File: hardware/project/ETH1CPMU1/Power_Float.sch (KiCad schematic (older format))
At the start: 53 parts, among them U601 TEL10-2415, U602 MC7815ABD2TR4G, U603 LM1117IMP-3.3/NOPB, U604 TSR1-2450, U605 LT8330_S6, U606 MC7915BD2TG, U607 LM1117IMP-5.0/NOPB, U608 TSR1-2490, U609 LT8330_S6

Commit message: Schematic design
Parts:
- added C628: 22u/16V, Capacitor_SMD:C_2220_5650Metric_Pad1.97x5.40mm_HandSolder, symbol Device:C
- added U610: LM1117IMP-3.3/NOPB, Package_TO_SOT_SMD:SOT-223-3_TabPin2, symbol Regulator_Linear:LM1117-3.3
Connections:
- net AGNDF: now also D602.1 (K), C628.2, U610.1 (GND)
- net at C609.1, U603.3 (VI), U604.3 (VO): now also U610.3 (VI)
- new net +3.3VP: C628.1, U610.2 (VO)
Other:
- moved on the sheet: C606, C617
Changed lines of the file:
@@
 Connection ~ 9350 3050
-Wire Wire Line
-	9350 3200 9350 3050
 Wire Wire Line
 	9350 3500 9350 3650
@@
 L Device:C C606
 U 1 1 5DD4C41A
-P 2600 3050
-F 0 "C606" V 2348 3050 50  0000 C CNN
-F 1 "1u" V 2439 3050 50  0000 C CNN
-F 2 "" H 2638 2900 50  0001 C CNN
-F 3 "~" H 2600 3050 50  0001 C CNN
-	1    2600 3050
+P 2650 3050
+F 0 "C606" V 2398 3050 50  0000 C CNN
+F 1 "1u" V 2489 3050 50  0000 C CNN
+F 2 "" H 2688 2900 50  0001 C CNN
+F 3 "~" H 2650 3050 50  0001 C CNN
+	1    2650 3050
 	0    1    1    0
 $EndComp
 Wire Wire Line
-	2450 3050 2350 3050
+	2500 3050 2350 3050
 Connection ~ 2350 3050
 Wire Wire Line
 	2850 3150 2850 3050
 Wire Wire Line
-	2750 3050 2850 3050
+	2800 3050 2850 3050
 Wire Wire Line
 	2850 3500 2850 3450
@@
 L Device:C C617
 U 1 1 5DE720A2
-P 2600 5200
-F 0 "C617" V 2348 5200 50  0000 C CNN
-F 1 "1u" V 2439 5200 50  0000 C CNN
-F 2 "" H 2638 5050 50  0001 C CNN
-F 3 "~" H 2600 5200 50  0001 C CNN
-	1    2600 5200
+P 2650 5200
+F 0 "C617" V 2398 5200 50  0000 C CNN
+F 1 "1u" V 2489 5200 50  0000 C CNN
+F 2 "" H 2688 5050 50  0001 C CNN
+F 3 "~" H 2650 5200 50  0001 C CNN
+	1    2650 5200
 	0    1    1    0
 $EndComp
 Wire Wire Line
-	2450 5200 2350 5200
+	2500 5200 2350 5200
 Connection ~ 2350 5200
 Wire Wire Line
 	2850 5300 2850 5200
 Wire Wire Line
-	2750 5200 2850 5200
+	2800 5200 2850 5200
 Wire Wire Line
 	2850 5650 2850 5600
@@
 Wire Wire Line
 	3350 1300 3950 1300
+$Comp
+L Regulator_Linear:LM1117-3.3 U?
+U 1 1 5E4B714B
+P 9900 1950
+AR Path="/5DC846AF/5E4B714B" Ref="U?"  Part="1"
+AR Path="/5DCE1F8B/5E4B714B" Ref="U?"  Part="1"
+AR Path="/5DD0DBE6/5E4B714B" Ref="U610"  Part="1"
+F 0 "U610" H 9900 2192 50  0000 C CNN
+F 1 "LM1117IMP-3.3/NOPB" H 9900 2100 50  0000 C CNN
+F 2 "Package_TO_SOT_SMD:SOT-223-3_TabPin2" H 9900 1950 50  0001 C CNN
+F 3 "http://www.ti.com/lit/ds/symlink/lm1117.pdf" H 9900 1950 50  0001 C CNN
+	1    9900 1950
+	1    0    0    -1
+$EndComp
+Wire Wire Line
+	9350 3200 9350 3050
+Wire Wire Line
+	9600 1950 9350 1950
+Wire Wire Line
+	9350 1950 9350 3050
+$Comp
+L Device:C C?
+U 1 1 5E4CE9DB
+P 10400 2250
+AR Path="/5DC846AF/5E4CE9DB" Ref="C?"  Part="1"
+AR Path="/5DCE1F8B/5E4CE9DB" Ref="C?"  Part="1"
+AR Path="/5DD0DBE6/5E4CE9DB" Ref="C628"  Part="1"
+F 0 "C628" H 10515 2296 50  0000 L CNN
+F 1 "22u/16V" H 10515 2205 50  0000 L CNN
+F 2 "Capacitor_SMD:C_2220_5650Metric_Pad1.97x5.40mm_HandSolder" H 10438 2100 50  0001 C CNN
+F 3 "~" H 10400 2250 50  0001 C CNN
+	1    10400 2250
+	1    0    0    -1
+$EndComp
+$Comp
+L ETH1CPMU1:DGNDF #PWR0622
+U 1 1 5E4E760E
+P 9900 2450
+F 0 "#PWR0622" H 9900 2200 50  0001 C CNN
+F 1 "DGNDF" H 9905 2277 50  0000 C CNN
+F 2 "" H 9900 2450 50  0001 C CNN
+F 3 "" H 9900 2450 50  0001 C CNN
+	1    9900 2450
+	1    0    0    -1
+$EndComp
+Wire Wire Line
+	9900 2450 9900 2250
+$Comp
+L ETH1CPMU1:DGNDF #PWR0623
+U 1 1 5E4F37FA
+P 10400 2450
+F 0 "#PWR0623" H 10400 2200 50  0001 C CNN
+F 1 "DGNDF" H 10405 2277 50  0000 C CNN
+F 2 "" H 10400 2450 50  0001 C CNN
+F 3 "" H 10400 2450 50  0001 C CNN
+	1    10400 2450
+	1    0    0    -1
+$EndComp
+Wire Wire Line
+	10400 2450 10400 2400
+Wire Wire Line
+	10400 2100 10400 1950
+Wire Wire Line
+	10400 1950 10200 1950
+$Comp
+L power:+3.3VP #PWR0621
+U 1 1 5E50E6BA
+P 10400 1800
+F 0 "#PWR0621" H 10550 1750 50  0001 C CNN
+F 1 "+3.3VP" H 10420 1943 50  0000 C CNN
+F 2 "" H 10400 1800 50  0001 C CNN
+F 3 "" H 10400 1800 50  0001 C CNN
+	1    10400 1800
+	1    0    0    -1
+$EndComp
+Wire Wire Line
+	10400 1800 10400 1950
+Connection ~ 10400 1950
+$Comp
+L ETH1CPMU1:DGNDF #PWR?
+U 1 1 5F7AA41C
+P 2850 5650
+F 0 "#PWR?" H 2850 5400 50  0001 C CNN
+F 1 "DGNDF" H 2855 5477 50  0000 C CNN
+F 2 "" H 2850 5650 50  0001 C CNN
+F 3 "" H 2850 5650 50  0001 C CNN
+	1    2850 5650
+	1    0    0    -1
+$EndComp
 $EndSCHEMATC

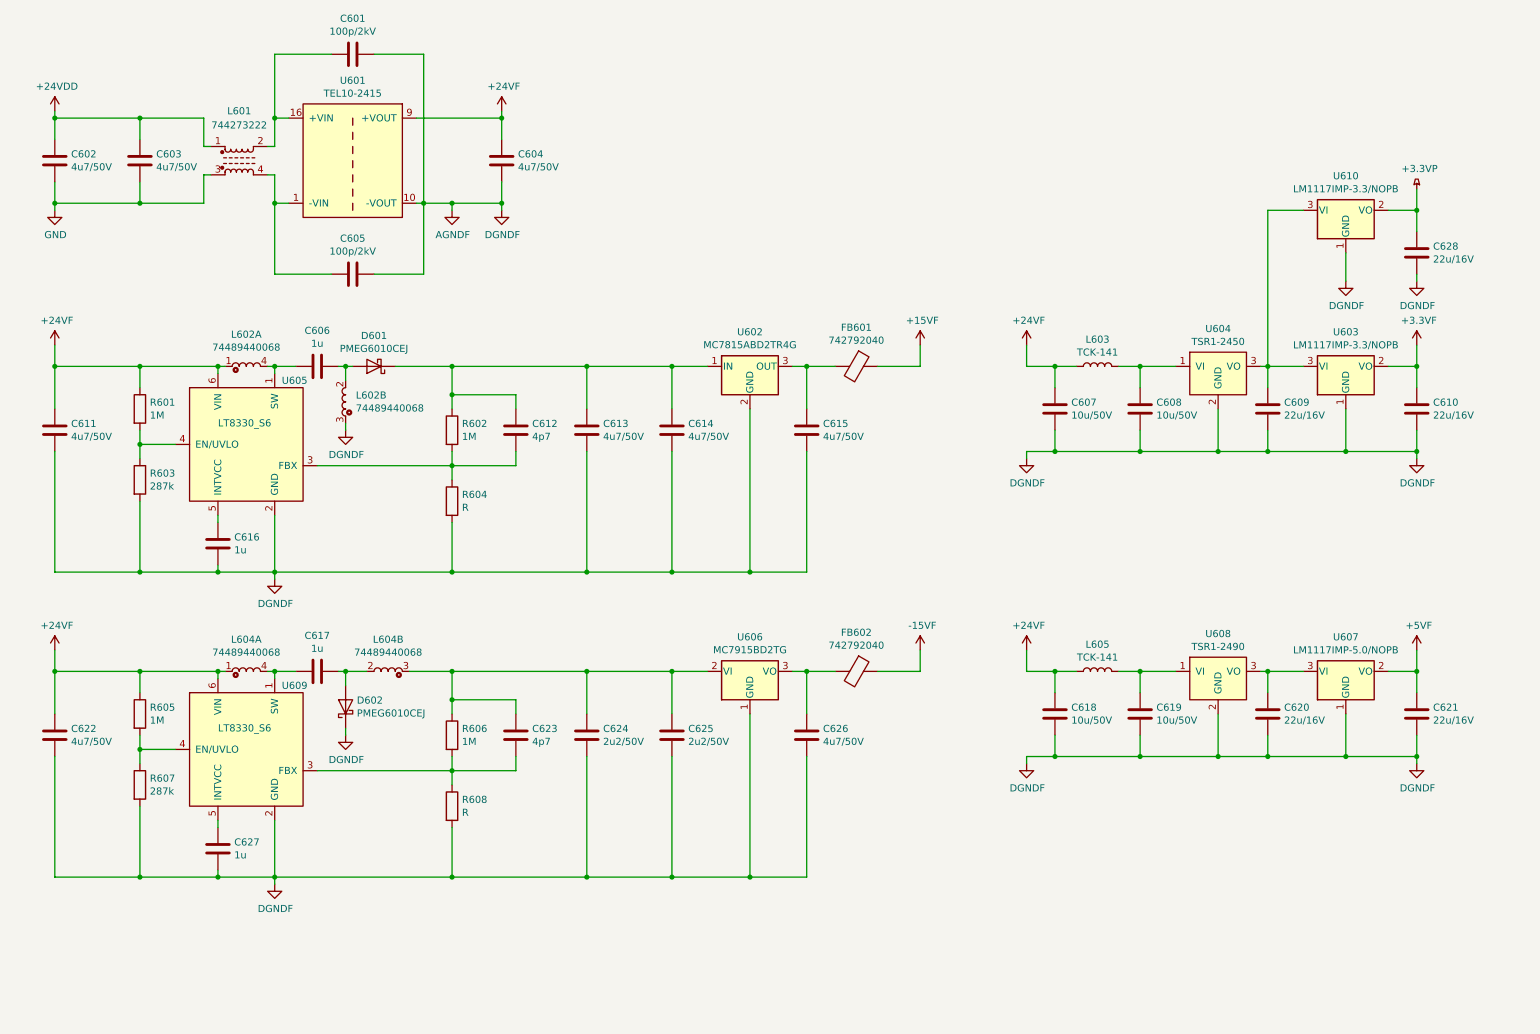
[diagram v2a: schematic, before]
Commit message: Function generator schematic design.
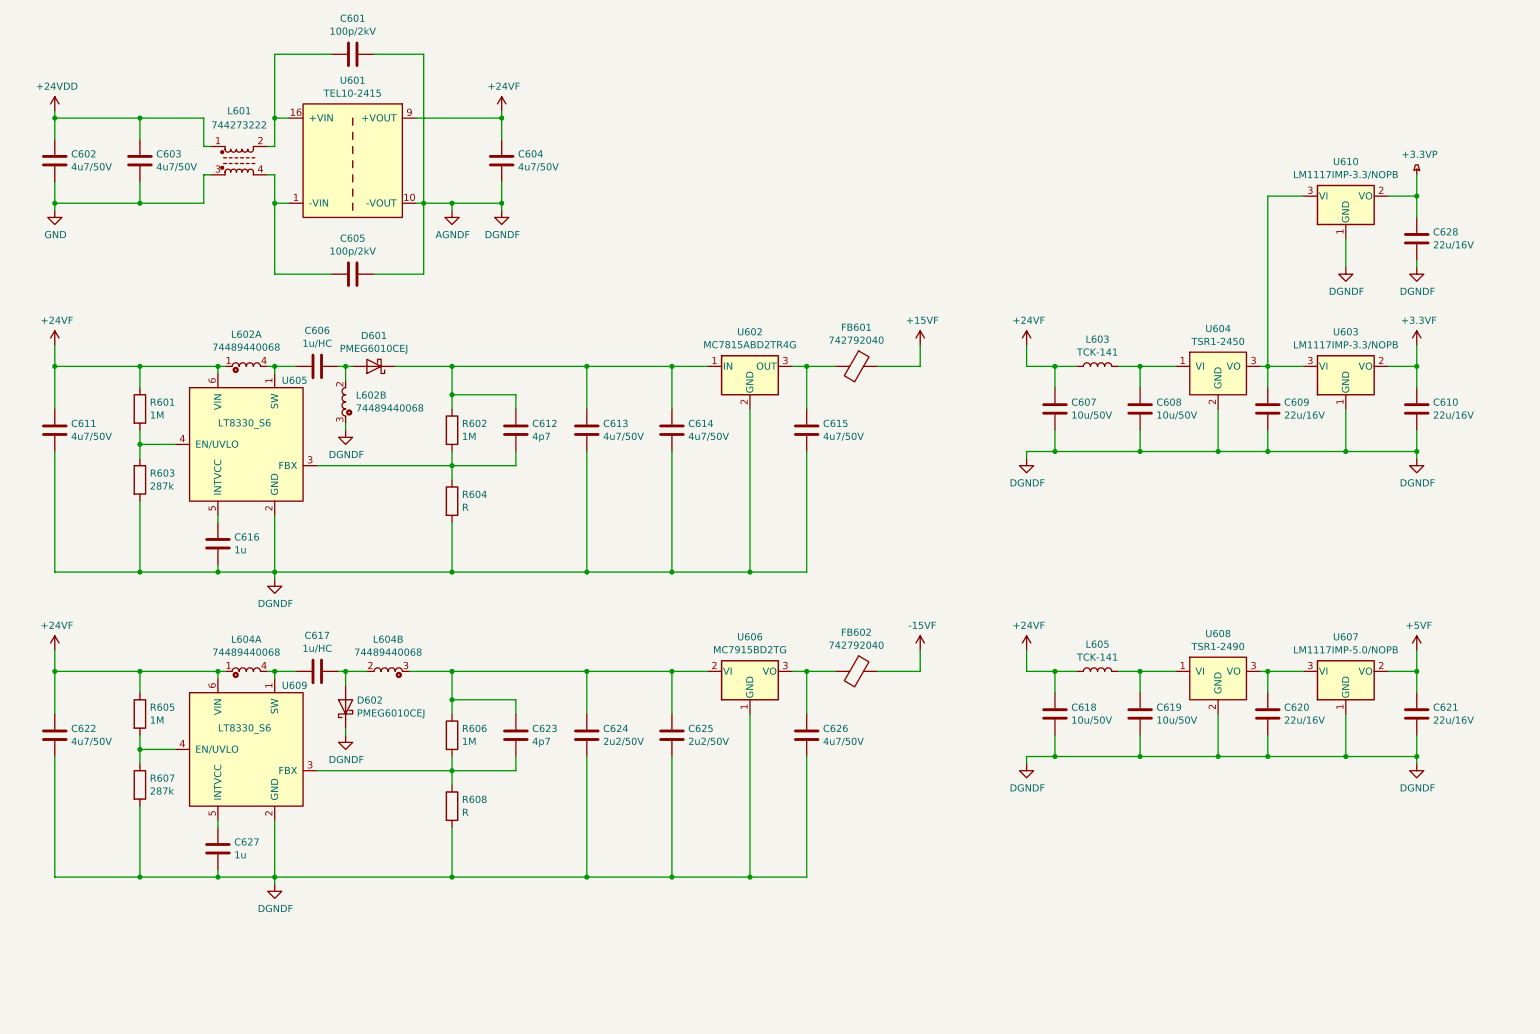
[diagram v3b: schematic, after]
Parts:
- C606, C617: value 1u -> 1u/HC
- C612, C616, C623, C627: footprint (none) -> Capacitor_SMD:C_0603_1608Metric_Pad1.05x0.95mm_HandSolder
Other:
- moved on the sheet: C628, U610
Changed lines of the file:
@@
 $Descr A4 11693 8268
 encoding utf-8
-Sheet 6 14
+Sheet 6 15
 Title ""
 Date ""
@@
 F 0 "C616" H 2065 4346 50  0000 L CNN
 F 1 "1u" H 2065 4255 50  0000 L CNN
-F 2 "" H 1988 4150 50  0001 C CNN
+F 2 "Capacitor_SMD:C_0603_1608Metric_Pad1.05x0.95mm_HandSolder" H 1988 4150 50  0001 C CNN
 F 3 "~" H 1950 4300 50  0001 C CNN
 	1    1950 4300
@@
 P 2650 3050
 F 0 "C606" V 2398 3050 50  0000 C CNN
-F 1 "1u" V 2489 3050 50  0000 C CNN
+F 1 "1u/HC" V 2489 3050 50  0000 C CNN
 F 2 "" H 2688 2900 50  0001 C CNN
 F 3 "~" H 2650 3050 50  0001 C CNN
@@
 F 0 "C612" H 4165 3546 50  0000 L CNN
 F 1 "4p7" H 4165 3455 50  0000 L CNN
-F 2 "" H 4088 3350 50  0001 C CNN
+F 2 "Capacitor_SMD:C_0603_1608Metric_Pad1.05x0.95mm_HandSolder" H 4088 3350 50  0001 C CNN
 F 3 "~" H 4050 3500 50  0001 C CNN
 	1    4050 3500
@@
 F 0 "C627" H 2065 6496 50  0000 L CNN
 F 1 "1u" H 2065 6405 50  0000 L CNN
-F 2 "" H 1988 6300 50  0001 C CNN
+F 2 "Capacitor_SMD:C_0603_1608Metric_Pad1.05x0.95mm_HandSolder" H 1988 6300 50  0001 C CNN
 F 3 "~" H 1950 6450 50  0001 C CNN
 	1    1950 6450
@@
 P 2650 5200
 F 0 "C617" V 2398 5200 50  0000 C CNN
-F 1 "1u" V 2489 5200 50  0000 C CNN
+F 1 "1u/HC" V 2489 5200 50  0000 C CNN
 F 2 "" H 2688 5050 50  0001 C CNN
 F 3 "~" H 2650 5200 50  0001 C CNN
@@
 F 0 "C623" H 4165 5696 50  0000 L CNN
 F 1 "4p7" H 4165 5605 50  0000 L CNN
-F 2 "" H 4088 5500 50  0001 C CNN
+F 2 "Capacitor_SMD:C_0603_1608Metric_Pad1.05x0.95mm_HandSolder" H 4088 5500 50  0001 C CNN
 F 3 "~" H 4050 5650 50  0001 C CNN
 	1    4050 5650
@@
 L Regulator_Linear:LM1117-3.3 U?
 U 1 1 5E4B714B
-P 9900 1950
+P 9900 1850
 AR Path="/5DC846AF/5E4B714B" Ref="U?"  Part="1"
 AR Path="/5DCE1F8B/5E4B714B" Ref="U?"  Part="1"
 AR Path="/5DD0DBE6/5E4B714B" Ref="U610"  Part="1"
-F 0 "U610" H 9900 2192 50  0000 C CNN
-F 1 "LM1117IMP-3.3/NOPB" H 9900 2100 50  0000 C CNN
-F 2 "Package_TO_SOT_SMD:SOT-223-3_TabPin2" H 9900 1950 50  0001 C CNN
-F 3 "http://www.ti.com/lit/ds/symlink/lm1117.pdf" H 9900 1950 50  0001 C CNN
-	1    9900 1950
+F 0 "U610" H 9900 2092 50  0000 C CNN
+F 1 "LM1117IMP-3.3/NOPB" H 9900 2000 50  0000 C CNN
+F 2 "Package_TO_SOT_SMD:SOT-223-3_TabPin2" H 9900 1850 50  0001 C CNN
+F 3 "http://www.ti.com/lit/ds/symlink/lm1117.pdf" H 9900 1850 50  0001 C CNN
+	1    9900 1850
 	1    0    0    -1
 $EndComp
@@
 	9350 3200 9350 3050
 Wire Wire Line
-	9600 1950 9350 1950
-Wire Wire Line
-	9350 1950 9350 3050
+	9600 1850 9350 1850
+Wire Wire Line
+	9350 1850 9350 3050
 $Comp
 L Device:C C?
 U 1 1 5E4CE9DB
-P 10400 2250
+P 10400 2150
 AR Path="/5DC846AF/5E4CE9DB" Ref="C?"  Part="1"
 AR Path="/5DCE1F8B/5E4CE9DB" Ref="C?"  Part="1"
 AR Path="/5DD0DBE6/5E4CE9DB" Ref="C628"  Part="1"
-F 0 "C628" H 10515 2296 50  0000 L CNN
-F 1 "22u/16V" H 10515 2205 50  0000 L CNN
-F 2 "Capacitor_SMD:C_2220_5650Metric_Pad1.97x5.40mm_HandSolder" H 10438 2100 50  0001 C CNN
-F 3 "~" H 10400 2250 50  0001 C CNN
-	1    10400 2250
+F 0 "C628" H 10515 2196 50  0000 L CNN
+F 1 "22u/16V" H 10515 2105 50  0000 L CNN
+F 2 "Capacitor_SMD:C_2220_5650Metric_Pad1.97x5.40mm_HandSolder" H 10438 2000 50  0001 C CNN
+F 3 "~" H 10400 2150 50  0001 C CNN
+	1    10400 2150
 	1    0    0    -1
 $EndComp
@@
 L ETH1CPMU1:DGNDF #PWR0622
 U 1 1 5E4E760E
-P 9900 2450
-F 0 "#PWR0622" H 9900 2200 50  0001 C CNN
-F 1 "DGNDF" H 9905 2277 50  0000 C CNN
-F 2 "" H 9900 2450 50  0001 C CNN
-F 3 "" H 9900 2450 50  0001 C CNN
-	1    9900 2450
-	1    0    0    -1
-$EndComp
-Wire Wire Line
-	9900 2450 9900 2250
+P 9900 2350
+F 0 "#PWR0622" H 9900 2100 50  0001 C CNN
+F 1 "DGNDF" H 9905 2177 50  0000 C CNN
+F 2 "" H 9900 2350 50  0001 C CNN
+F 3 "" H 9900 2350 50  0001 C CNN
+	1    9900 2350
+	1    0    0    -1
+$EndComp
+Wire Wire Line
+	9900 2350 9900 2150
 $Comp
 L ETH1CPMU1:DGNDF #PWR0623
 U 1 1 5E4F37FA
-P 10400 2450
-F 0 "#PWR0623" H 10400 2200 50  0001 C CNN
-F 1 "DGNDF" H 10405 2277 50  0000 C CNN
-F 2 "" H 10400 2450 50  0001 C CNN
-F 3 "" H 10400 2450 50  0001 C CNN
-	1    10400 2450
-	1    0    0    -1
-$EndComp
-Wire Wire Line
-	10400 2450 10400 2400
-Wire Wire Line
-	10400 2100 10400 1950
-Wire Wire Line
-	10400 1950 10200 1950
+P 10400 2350
+F 0 "#PWR0623" H 10400 2100 50  0001 C CNN
+F 1 "DGNDF" H 10405 2177 50  0000 C CNN
+F 2 "" H 10400 2350 50  0001 C CNN
+F 3 "" H 10400 2350 50  0001 C CNN
+	1    10400 2350
+	1    0    0    -1
+$EndComp
+Wire Wire Line
+	10400 2350 10400 2300
+Wire Wire Line
+	10400 2000 10400 1850
+Wire Wire Line
+	10400 1850 10200 1850
 $Comp
 L power:+3.3VP #PWR0621
 U 1 1 5E50E6BA
-P 10400 1800
-F 0 "#PWR0621" H 10550 1750 50  0001 C CNN
-F 1 "+3.3VP" H 10420 1943 50  0000 C CNN
-F 2 "" H 10400 1800 50  0001 C CNN
-F 3 "" H 10400 1800 50  0001 C CNN
-	1    10400 1800
-	1    0    0    -1
-$EndComp
-Wire Wire Line
-	10400 1800 10400 1950
-Connection ~ 10400 1950
-$Comp
-L ETH1CPMU1:DGNDF #PWR?
+P 10400 1700
+F 0 "#PWR0621" H 10550 1650 50  0001 C CNN
+F 1 "+3.3VP" H 10420 1843 50  0000 C CNN
+F 2 "" H 10400 1700 50  0001 C CNN
+F 3 "" H 10400 1700 50  0001 C CNN
+	1    10400 1700
+	1    0    0    -1
+$EndComp
+Wire Wire Line
+	10400 1700 10400 1850
+Connection ~ 10400 1850
+$Comp
+L ETH1CPMU1:DGNDF #PWR0624
 U 1 1 5F7AA41C
 P 2850 5650
-F 0 "#PWR?" H 2850 5400 50  0001 C CNN
+F 0 "#PWR0624" H 2850 5400 50  0001 C CNN
 F 1 "DGNDF" H 2855 5477 50  0000 C CNN
 F 2 "" H 2850 5650 50  0001 C CNN

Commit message: Function generator schematic development.
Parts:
- R601, R602, R603, R604, R605, R606, R607, R608: footprint (none) -> Resistor_SMD:R_0603_1608Metric_Pad1.05x0.95mm_HandSolder
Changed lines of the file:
@@
 EESchema Schematic File Version 4
-LIBS:ETH1CPMU1-cache
 EELAYER 30 0
 EELAYER END
@@
 F 0 "R601" H 1470 3396 50  0000 L CNN
 F 1 "1M" H 1470 3305 50  0000 L CNN
-F 2 "" V 1330 3350 50  0001 C CNN
+F 2 "Resistor_SMD:R_0603_1608Metric_Pad1.05x0.95mm_HandSolder" V 1330 3350 50  0001 C CNN
 F 3 "~" H 1400 3350 50  0001 C CNN
 	1    1400 3350
@@
 F 0 "R603" H 1470 3896 50  0000 L CNN
 F 1 "287k" H 1470 3805 50  0000 L CNN
-F 2 "" V 1330 3850 50  0001 C CNN
+F 2 "Resistor_SMD:R_0603_1608Metric_Pad1.05x0.95mm_HandSolder" V 1330 3850 50  0001 C CNN
 F 3 "~" H 1400 3850 50  0001 C CNN
 	1    1400 3850
@@
 F 0 "R604" H 3670 4046 50  0000 L CNN
 F 1 "R" H 3670 3955 50  0000 L CNN
-F 2 "" V 3530 4000 50  0001 C CNN
+F 2 "Resistor_SMD:R_0603_1608Metric_Pad1.05x0.95mm_HandSolder" V 3530 4000 50  0001 C CNN
 F 3 "~" H 3600 4000 50  0001 C CNN
 	1    3600 4000
@@
 F 0 "R602" H 3670 3546 50  0000 L CNN
 F 1 "1M" H 3670 3455 50  0000 L CNN
-F 2 "" V 3530 3500 50  0001 C CNN
+F 2 "Resistor_SMD:R_0603_1608Metric_Pad1.05x0.95mm_HandSolder" V 3530 3500 50  0001 C CNN
 F 3 "~" H 3600 3500 50  0001 C CNN
 	1    3600 3500
@@
 F 0 "R605" H 1470 5546 50  0000 L CNN
 F 1 "1M" H 1470 5455 50  0000 L CNN
-F 2 "" V 1330 5500 50  0001 C CNN
+F 2 "Resistor_SMD:R_0603_1608Metric_Pad1.05x0.95mm_HandSolder" V 1330 5500 50  0001 C CNN
 F 3 "~" H 1400 5500 50  0001 C CNN
 	1    1400 5500
@@
 F 0 "R607" H 1470 6046 50  0000 L CNN
 F 1 "287k" H 1470 5955 50  0000 L CNN
-F 2 "" V 1330 6000 50  0001 C CNN
+F 2 "Resistor_SMD:R_0603_1608Metric_Pad1.05x0.95mm_HandSolder" V 1330 6000 50  0001 C CNN
 F 3 "~" H 1400 6000 50  0001 C CNN
 	1    1400 6000
@@
 F 0 "R608" H 3670 6196 50  0000 L CNN
 F 1 "R" H 3670 6105 50  0000 L CNN
-F 2 "" V 3530 6150 50  0001 C CNN
+F 2 "Resistor_SMD:R_0603_1608Metric_Pad1.05x0.95mm_HandSolder" V 3530 6150 50  0001 C CNN
 F 3 "~" H 3600 6150 50  0001 C CNN
 	1    3600 6150
@@
 F 0 "R606" H 3670 5696 50  0000 L CNN
 F 1 "1M" H 3670 5605 50  0000 L CNN
-F 2 "" V 3530 5650 50  0001 C CNN
+F 2 "Resistor_SMD:R_0603_1608Metric_Pad1.05x0.95mm_HandSolder" V 3530 5650 50  0001 C CNN
 F 3 "~" H 3600 5650 50  0001 C CNN
 	1    3600 5650

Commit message: Power schematic update.
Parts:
- removed L601: 744273222, ETH1CPMU1:744273222, symbol Device:L_Core_Ferrite_Coupled
- removed U601: TEL10-2415, symbol ETH1CPMU1:TEL10-2415
- added L601: 7448013501, symbol ETH1CPMU1:7448013501
- added U601: THL15-2415WI, symbol ETH1CPMU1:THL15-2415WI
- C601, C605: value 100p/2kV -> 330p/2kV
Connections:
- net +24VDD: now also L601.1
- net +24VF: now also U601.3 (+VOUT)
- net AGNDF: now also U601.5 (-VOUT)
- net GND: now also L601.2
- net at C601.2: now also L601.4, U601.1 (+VIN)
- net at C605.2: now also L601.3, U601.2 (-VIN)
- no-connect marks 0 -> 2
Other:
- moved on the sheet: C601, C604, C605, C606, C607, C608, C609, C610, C611, C612, C613, C614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

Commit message: New footprint development, changes in schematics.
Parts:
- removed U604: TSR1-2450, symbol ETH1CPMU1:TSR1-2450
- added C608, C611: 10u/50V, Capacitor_SMD:C_1210_3225Metric_Pad1.42x2.65mm_HandSolder, symbol Device:C
- added U605: TSR2-2450, symbol ETH1CPMU1:TSR2
- C601, C602, C603, C604: footprint (none) -> Capacitor_SMD:C_1206_3216Metric_Pad1.42x1.75mm_HandSolder
- C606: renamed from C605; footprint (none) -> Capacitor_SMD:C_1206_3216Metric_Pad1.42x1.75mm_HandSolder
- C609: renamed from C607; footprint (none) -> Capacitor_SMD:C_1210_3225Metric_Pad1.42x2.65mm_HandSolder
- C610: renamed from C608; footprint Capacitor_SMD:C_2220_5650Metric_Pad1.97x5.40mm_HandSolder -> Capacitor_SMD:C_1210_3225Metric_Pad1.42x2.65mm_HandSolder
- C614: renamed from C611; footprint (none) -> Capacitor_SMD:C_1206_3216Metric_Pad1.42x1.75mm_HandSolder
- C616: renamed from C613; footprint (none) -> Capacitor_SMD:C_1206_3216Metric_Pad1.42x1.75mm_HandSolder
- C617: renamed from C614; footprint (none) -> Capacitor_SMD:C_1206_3216Metric_Pad1.42x1.75mm_HandSolder
- C618: renamed from C615; footprint (none) -> Capacitor_SMD:C_1206_3216Metric_Pad1.42x1.75mm_HandSolder
- C621: renamed from C618; footprint (none) -> Capacitor_SMD:C_1210_3225Metric_Pad1.42x2.65mm_HandSolder
- C622: renamed from C619; footprint Capacitor_SMD:C_2220_5650Metric_Pad1.97x5.40mm_HandSolder -> Capacitor_SMD:C_1210_3225Metric_Pad1.42x2.65mm_HandSolder
- C625: renamed from C622; footprint (none) -> Capacitor_SMD:C_1206_3216Metric_Pad1.42x1.75mm_HandSolder
- C627: renamed from C624; footprint (none) -> Capacitor_SMD:C_0805_2012Metric_Pad1.15x1.40mm_HandSolder
- C628: renamed from C625; footprint (none) -> Capacitor_SMD:C_0805_2012Metric_Pad1.15x1.40mm_HandSolder
- C629: renamed from C626; footprint (none) -> Capacitor_SMD:C_1206_3216Metric_Pad1.42x1.75mm_HandSolder
- D601, D602: footprint (none) -> Diode_SMD:D_SOD-323_HandSoldering
- FB601, FB602: value 742792040 -> 742792031; footprint (none) -> Inductor_SMD:L_0805_2012Metric_Pad1.15x1.40mm_HandSolder
- L602, L604: footprint (none) -> ETH1CPMU1:74489440068
- U603: renamed from U602; value MC7815ABD2TR4G -> MC7815BD2TG; footprint (none) -> Package_TO_SOT_SMD:TO-263-2
- U606: renamed from U605; footprint (none) -> Package_TO_SOT_SMD:TSOT-23-6_HandSoldering
- U607: renamed from U606; footprint (none) -> Package_TO_SOT_SMD:TO-263-2
- U610: renamed from U609; footprint (none) -> Package_TO_SOT_SMD:TSOT-23-6_HandSoldering
- renumbered C628 to C605, C606 to C607, C609 to C612, C610 to C613, C612 to C615, C616 to C619, C617 to C620, C620 to C623, C621 to C624, C623 to C626, C627 to C630, U610 to U602, U603 to U604, U607 to U608, U608 to U609
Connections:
- net +24VF: now also C608.1
- net AGNDF: now also C608.2, C611.2, U605.2 (GND)
- net at C612.1, U602.3 (VI), U604.3 (VI): now also U605.3 (VO)
- net at C610.1, L603.2: now also C611.1, U605.1 (VI)
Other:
- moved on the sheet: C601, C602, C603, C604, C605, C606, C607, C609, C610, C612, C613, C614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
